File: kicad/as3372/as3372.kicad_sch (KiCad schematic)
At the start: 27 parts, among them J1 Conn_01x01, J2 Conn_01x02, J3 Conn_02x20_Odd_Even, U1 MUX508, U15 M24C02-WMN, U2 MUX508, U3 NE5532, U7 CAT9555YI-T2

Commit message: start placing
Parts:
- removed H2, H4: MountingHole, MountingHole:MountingHole_3.2mm_M3, symbol Mechanical:MountingHole
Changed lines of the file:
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@@
-    )
-  )
-  (symbol (lib_id "Mechanical:MountingHole") (at 360.68 38.1 0) (unit 1)
-    (in_bom yes) (on_board yes)
-    (property "Reference" "H4" (id 0) (at 363.22 36.9316 0)
-      (effects (font (size 1.27 1.27)) (justify left))
-    )
-    (property "Value" "MountingHole" (id 1) (at 363.22 39.243 0)
-      (effects (font (size 1.27 1.27)) (justify left))
-    )
-    (property "Footprint" "MountingHole:MountingHole_3.2mm_M3" (id 2) (at 360.68 38.1 0)
-      (effects (font (size 1.27 1.27)) hide)
-    )
-    (property "Datasheet" "~" (id 3) (at 360.68 38.1 0)
-      (effects (font (size 1.27 1.27)) hide)
-    )
-  )
-  (symbol (lib_id "Mechanical:MountingHole") (at 346.71 38.1 0) (unit 1)
-    (in_bom yes) (on_board yes)
-    (property "Reference" "H2" (id 0) (at 349.25 36.9316 0)
-      (effects (font (size 1.27 1.27)) (justify left))
-    )
-    (property "Value" "MountingHole" (id 1) (at 349.25 39.243 0)
-      (effects (font (size 1.27 1.27)) (justify left))
-    )
-    (property "Footprint" "MountingHole:MountingHole_3.2mm_M3" (id 2) (at 346.71 38.1 0)
-      (effects (font (size 1.27 1.27)) hide)
-    )
-    (property "Datasheet" "~" (id 3) (at 346.71 38.1 0)
-      (effects (font (size 1.27 1.27)) hide)
     )
   )
@@
       (reference "H1") (unit 1) (value "MountingHole") (footprint "MountingHole:MountingHole_3.2mm_M3")
     )
-    (path "/00000000-0000-0000-0000-0000640c295f"
-      (reference "H2") (unit 1) (value "MountingHole") (footprint "MountingHole:MountingHole_3.2mm_M3")
-    )
     (path "/00000000-0000-0000-0000-0000640c1f92"
       (reference "H3") (unit 1) (value "MountingHole") (footprint "MountingHole:MountingHole_3.2mm_M3")
     )
-    (path "/00000000-0000-0000-0000-0000640c239a"
-      (reference "H4") (unit 1) (value "MountingHole") (footprint "MountingHole:MountingHole_3.2mm_M3")
-    )
     (path "/3bdd9acf-e624-46b6-8487-c2e2595a6ff3"

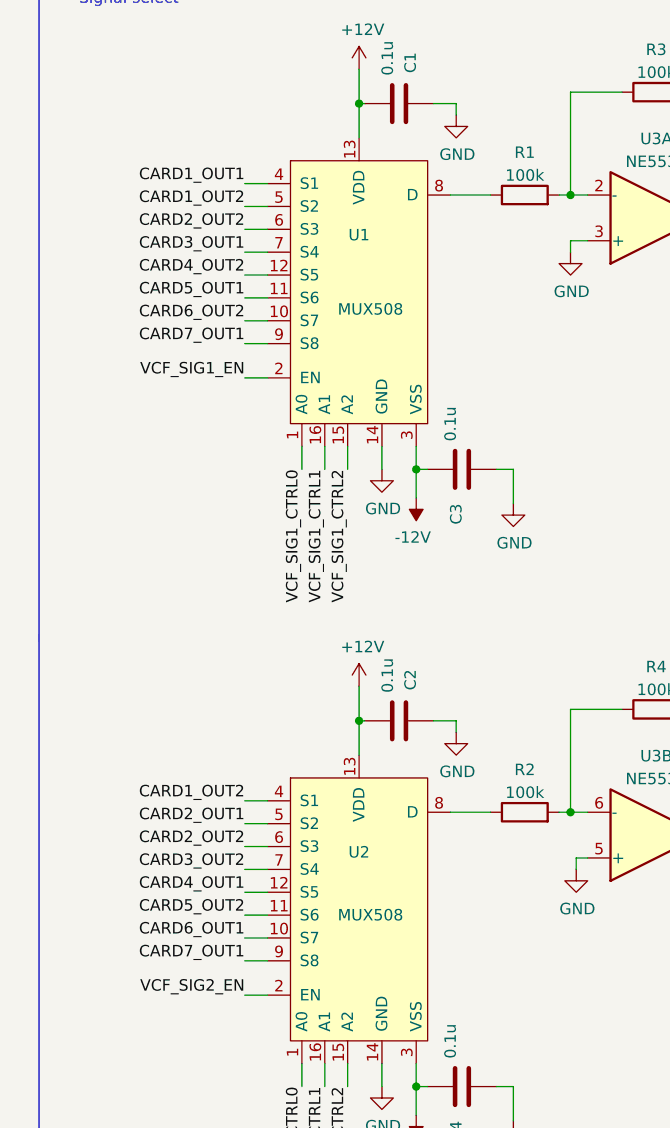
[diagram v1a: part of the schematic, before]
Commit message: having a tough time routing full filter with modes
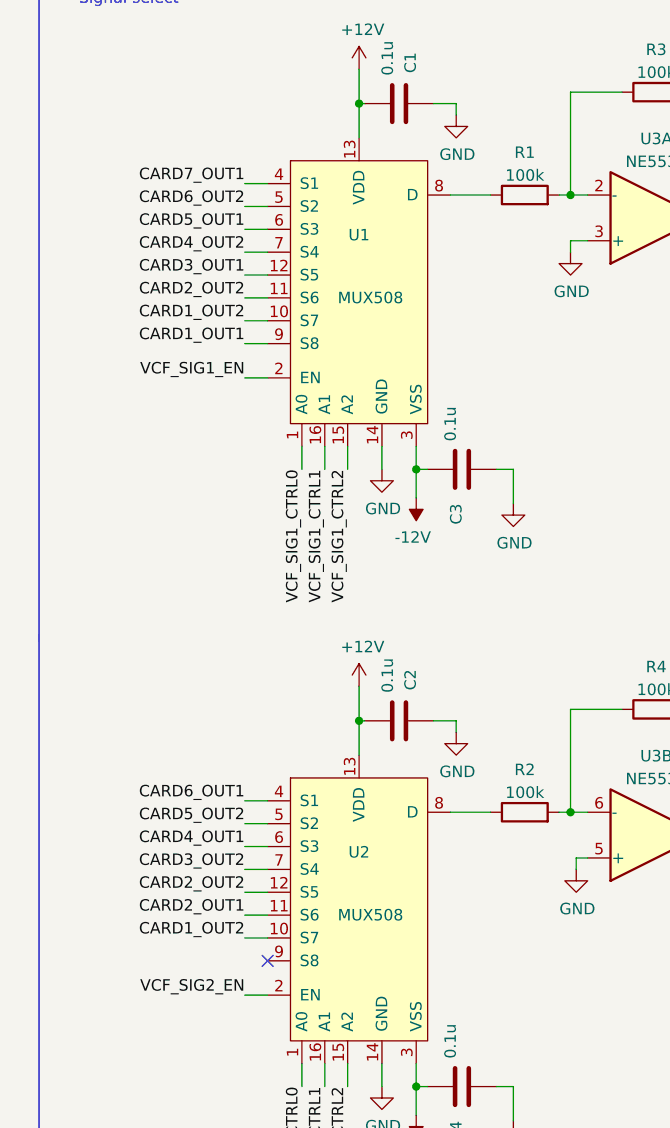
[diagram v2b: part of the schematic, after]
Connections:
- net CARD1_OUT1: now also U1.9 (S8); no longer U1.4 (S1)
- net CARD1_OUT2: now also U1.10 (S7), U2.10 (S7); no longer U1.5 (S2), U2.4 (S1)
- net CARD2_OUT1: now also U2.11 (S6); no longer U2.5 (S2)
- net CARD2_OUT2: now also U1.11 (S6), U2.12 (S5); no longer U1.6 (S3), U2.6 (S3)
- net CARD3_OUT1: now also U1.12 (S5); no longer U1.7 (S4)
- net CARD4_OUT1: now also U2.6 (S3); no longer U2.12 (S5)
- net CARD4_OUT2: now also U1.7 (S4); no longer U1.12 (S5)
- net CARD5_OUT1: now also U1.6 (S3); no longer U1.11 (S6)
- net CARD5_OUT2: now also U2.5 (S2); no longer U2.11 (S6)
- net CARD6_OUT1: now also U2.4 (S1); no longer U2.10 (S7)
- net CARD6_OUT2: now also U1.5 (S2); no longer U1.10 (S7)
- net CARD7_OUT1: now also U1.4 (S1); no longer U1.9 (S8), U2.9 (S8)
- no-connect marks 3 -> 4

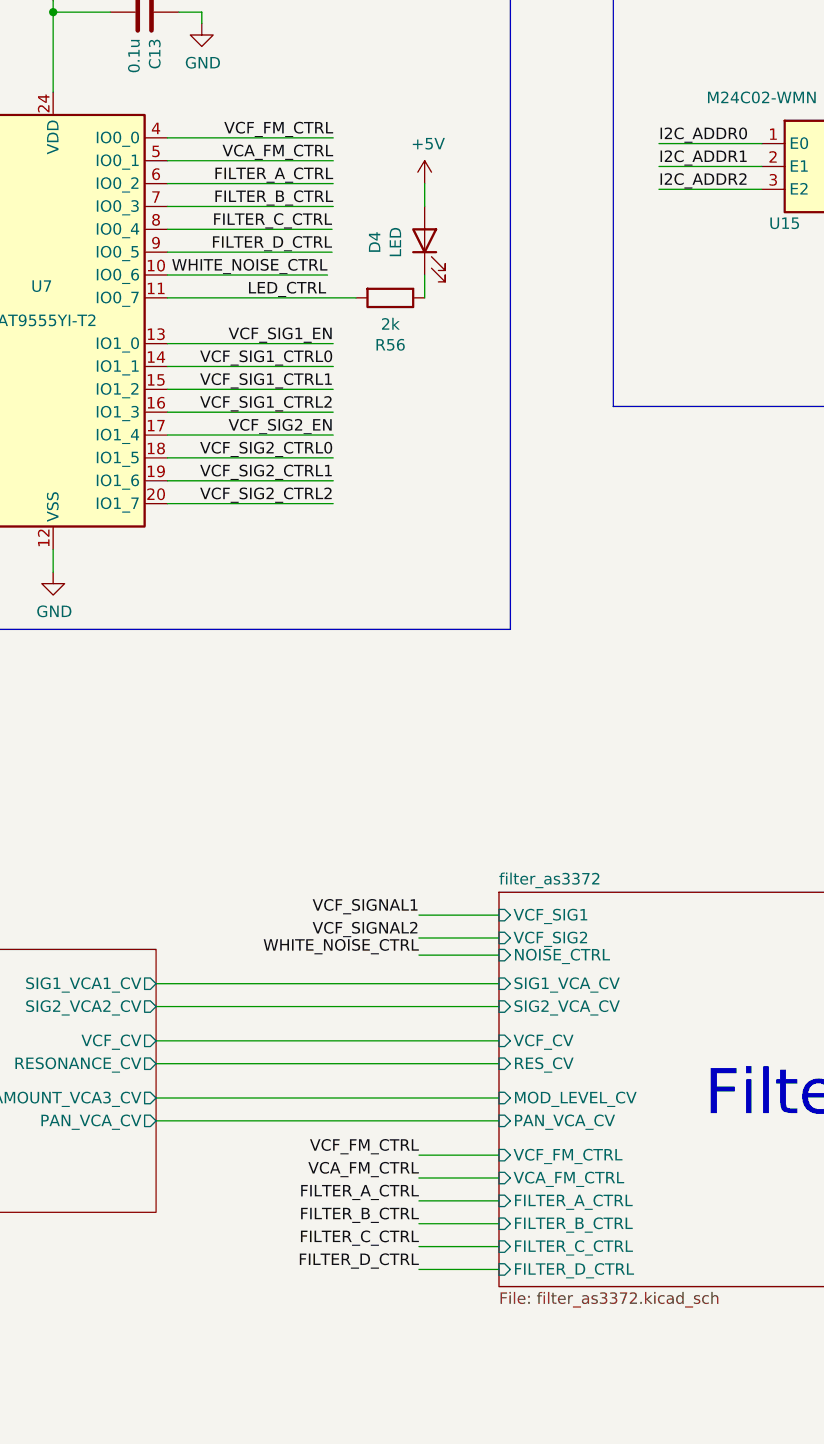
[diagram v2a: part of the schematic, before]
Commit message: simplify and remove filter mode select
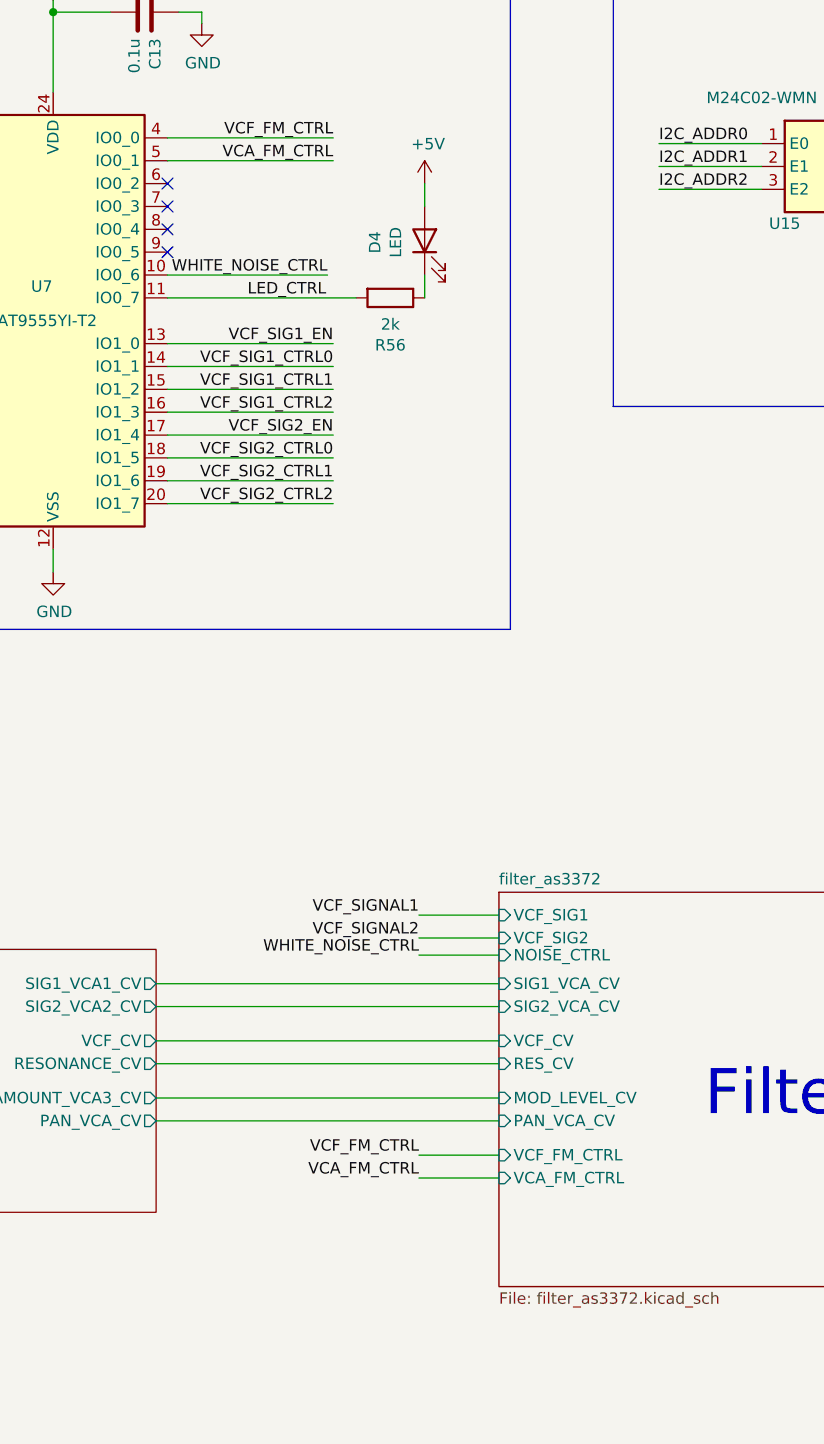
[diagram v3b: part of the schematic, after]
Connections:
- net FILTER_A_CTRL: no longer names the net of U7.6 (IO0_2)
- net FILTER_B_CTRL: no longer names the net of U7.7 (IO0_3)
- net FILTER_C_CTRL: no longer names the net of U7.8 (IO0_4)
- net FILTER_D_CTRL: no longer names the net of U7.9 (IO0_5)
- no-connect marks 4 -> 8
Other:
- sheet filter_as3372 ports: added none; removed FILTER_A_CTRL, FILTER_B_CTRL, FILTER_C_CTRL, FILTER_D_CTRL

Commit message: routing done needs review
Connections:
- net CARD1_OUT1: now also U2.9 (S8)
- net LED_CTRL: now also U7.6 (IO0_2); no longer U7.11 (IO0_7)
- no-connect marks 8 -> 7
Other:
- moved on the sheet: C1, C2, C3, C37, C4, C5, C6, D4, J1, J2, R1, R2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

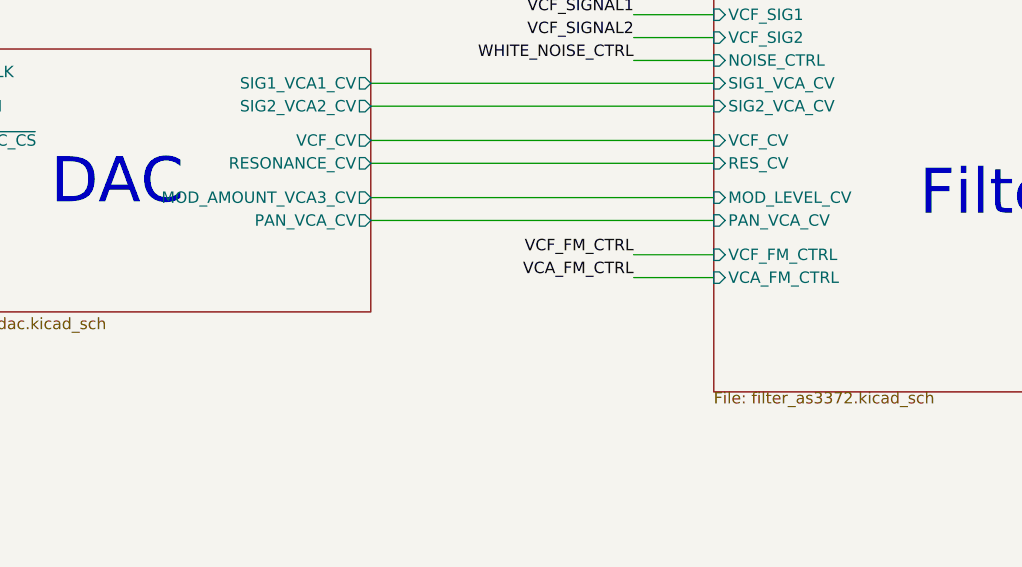
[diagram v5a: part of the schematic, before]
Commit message: add white noise enable/powerdown
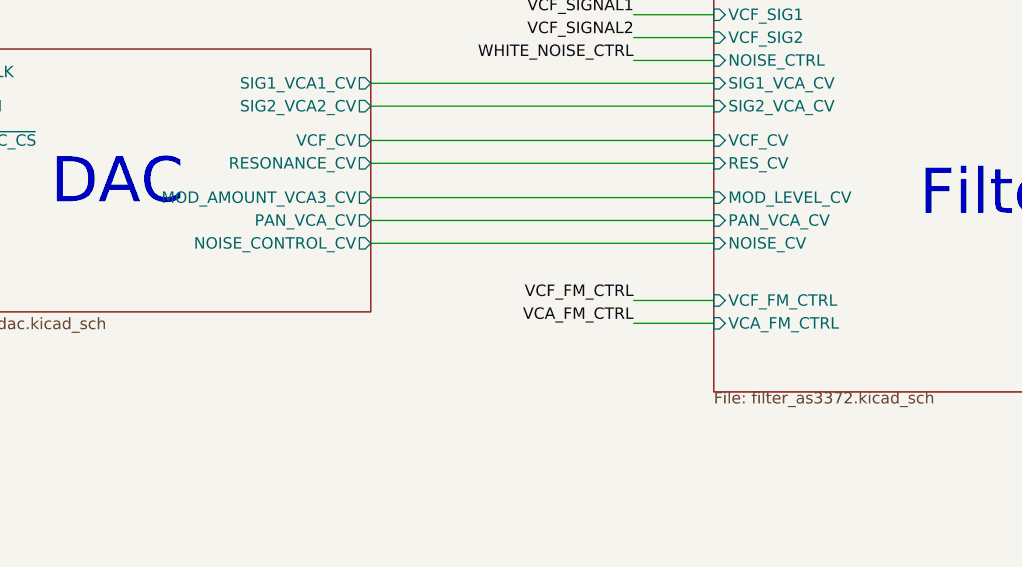
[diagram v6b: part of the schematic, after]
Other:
- sheet DAC ports: added NOISE_CONTROL_CV; removed none
- sheet filter_as3372 ports: added NOISE_CV; removed none
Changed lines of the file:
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@@
+    (stroke (width 0) (type default) (color 0 0 0 0))
+  )
+  (wire (pts (xy 191.77 156.21) (xy 229.87 156.21))
     (stroke (width 0) (type default) (color 0 0 0 0))
   )
@@
     (stroke (width 0) (type default) (color 0 0 0 0))
   )
-  (wire (pts (xy 220.98 157.48) (xy 229.87 157.48))
+  (wire (pts (xy 220.98 162.56) (xy 229.87 162.56))
     (stroke (width 0) (type default) (color 0 0 0 0))
   )
@@
     (stroke (width 0) (type default) (color 0 0 0 0))
   )
-  (wire (pts (xy 220.98 160.02) (xy 229.87 160.02))
+  (wire (pts (xy 220.98 165.1) (xy 229.87 165.1))
     (stroke (width 0) (type default) (color 0 0 0 0))
   )
@@
     (effects (font (size 1.27 1.27)) (justify right bottom))
   )
-  (label "VCF_FM_CTRL" (at 220.98 157.48 180)
+  (label "VCF_FM_CTRL" (at 220.98 162.56 180)
     (effects (font (size 1.27 1.27)) (justify right bottom))
   )
@@
     (effects (font (size 1.27 1.27)) (justify right bottom))
   )
-  (label "VCA_FM_CTRL" (at 220.98 160.02 180)
+  (label "VCA_FM_CTRL" (at 220.98 165.1 180)
     (effects (font (size 1.27 1.27)) (justify right bottom))
   )
@@
       (effects (font (size 1.27 1.27)) (justify right))
     )
+    (pin "NOISE_CONTROL_CV" output (at 191.77 156.21 0)
+      (effects (font (size 1.27 1.27)) (justify right))
+    )
   )
   (sheet (at 229.87 128.27) (size 64.77 44.45) (fields_autoplaced)
@@
       (effects (font (size 1.27 1.27)) (justify left))
     )
-    (pin "VCF_FM_CTRL" input (at 229.87 157.48 180)
-      (effects (font (size 1.27 1.27)) (justify left))
-    )
-    (pin "VCA_FM_CTRL" input (at 229.87 160.02 180)
+    (pin "VCF_FM_CTRL" input (at 229.87 162.56 180)
+      (effects (font (size 1.27 1.27)) (justify left))
+    )
+    (pin "VCA_FM_CTRL" input (at 229.87 165.1 180)
       (effects (font (size 1.27 1.27)) (justify left))
     )
@@
     )
     (pin "NOISE_CTRL" input (at 229.87 135.89 180)
+      (effects (font (size 1.27 1.27)) (justify left))
+    )
+    (pin "NOISE_CV" input (at 229.87 156.21 180)
       (effects (font (size 1.27 1.27)) (justify left))
     )
@@
       (reference "#PWR028") (unit 1) (value "GND") (footprint "")
     )
+    (path "/06519ee5-e3f7-4c1d-97d6-a8703fead30d/6ee86ae3-2656-4f63-9de6-e42b5b322983"
+      (reference "#PWR029") (unit 1) (value "GND") (footprint "")
+    )
     (path "/00000000-0000-0000-0000-000061ff2290/00000000-0000-0000-0000-0000622965dc"
       (reference "#PWR031") (unit 1) (value "+5V") (footprint "")
@@
       (reference "Q2") (unit 1) (value "MMBT3904") (footprint "Package_TO_SOT_SMD:SOT-23")
     )
+    (path "/06519ee5-e3f7-4c1d-97d6-a8703fead30d/55e53c3f-c971-4f19-922b-002bf51246f9"
+      (reference "Q3") (unit 1) (value "MMBT3904") (footprint "Package_TO_SOT_SMD:SOT-23")
+    )
     (path "/48ba0279-7271-4ec0-ba38-a30055ac9f59"
       (reference "R1") (unit 1) (value "100k") (footprint "Resistor_SMD:R_0402_1005Metric")
@@
       (reference "R15") (unit 1) (value "36k") (footprint "Resistor_SMD:R_0603_1608Metric")
     )
+    (path "/06519ee5-e3f7-4c1d-97d6-a8703fead30d/a9d46dee-3686-4e76-af83-0df79a10f957"
+      (reference "R16") (unit 1) (value "1k") (footprint "Resistor_SMD:R_0603_1608Metric")
+    )
     (path "/06519ee5-e3f7-4c1d-97d6-a8703fead30d/64293c9e-1637-4502-9e62-b413bb4bd05d"
       (reference "R18") (unit 1) (value "68k") (footprint "Resistor_SMD:R_0603_1608Metric")
@@
       (reference "TP13") (unit 1) (value "TestPoint") (footprint "TestPoint:TestPoint_Pad_2.0x2.0mm")
     )
-    (path "/00000000-0000-0000-0000-000061ff2290/a3ab1928-335f-4dcb-9beb-d7ee33a5ecd6"
-      (reference "TP14") (unit 1) (value "TestPoint") (footprint "TestPoint:TestPoint_Pad_2.0x2.0mm")
-    )
     (path "/06519ee5-e3f7-4c1d-97d6-a8703fead30d/802ac57d-6976-435d-bbe0-454dcb59ad4a"

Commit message: schematic updated
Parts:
- removed U3: NE5532, Package_SO:SOIC-8_3.9x4.9mm_P1.27mm, symbol Amplifier_Operational:NE5532
- added C21: 0.1u, Capacitor_SMD:C_0603_1608Metric, symbol Device:C
- added Q4: MMBT3904, Package_TO_SOT_SMD:SOT-23, symbol Transistor_BJT:MMBT3904
- added R17: 100, Resistor_SMD:R_0805_2012Metric, symbol Device:R
- added U3: TL074, Package_SO:SOIC-14_3.9x8.7mm_P1.27mm, symbol Amplifier_Operational:TL074
- R3, R4: value 100k -> 1k; footprint Resistor_SMD:R_0402_1005Metric -> Resistor_SMD:R_0805_2012Metric; LCSC Part C25741 -> C17513
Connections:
- net +12V: now also U3.4 (V+)
- net +5V: now also R4.2
- net -12V: now also U3.11 (V-)
- net GND: now also R1.1, R2.1, C21.2, Q4.2 (E), U3.12 (+)
- net GPIO_MODULE_DRIVEN: now also R17.2
- net VCF_SIGNAL1: now also U3.6 (-), U3.7; no longer R3.2
- net VCF_SIGNAL2: now also U3.1, U3.2 (-); no longer R4.2
- net at R3.1: now also U3.8, U3.9 (-); no longer R1.2
- net at R4.1: now also Q4.3 (C), R17.1; no longer R2.2
- net at U1.8 (D): now also R1.2, U3.5 (+); no longer R1.1
- net at U2.8 (D): now also R2.2, U3.3 (+); no longer R2.1
- new net: C21.1, Q4.1 (B), R3.2
- new net: U3.13 (-), U3.14
- new net VCF_RAW: U3.10 (+)
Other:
- sheet filter_as3372 ports: added VCF_RAW; removed none
- note added: "GPIO Module Driven: Take VCF output to drive a switch. Used to calibrate the noise source or resonanance level. And yes, it's inverted. You can do it. Cap gives a decent capability to detect via interrupt whether a signal is being generated or not. The diode is questionable..."
- note added: "Signal select -- output selected signal in-phase"
- note removed: "Signal select"
- moved on the sheet: R1, R2

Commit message: updates for v0.2
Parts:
- added H2, H4: MountingHole, MountingHole:MountingHole_3.2mm_M3, symbol Mechanical:MountingHole
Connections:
- net GND: now also U3.5 (+); no longer U3.12 (+)
- net VCA_FM_CTRL: now also U7.8 (IO0_4); no longer U7.5 (IO0_1)
- net VCF_SIGNAL1: now also U3.13 (-), U3.14; no longer U3.6 (-), U3.7
- net at R1.2, U1.8 (D): now also U3.12 (+); no longer U3.5 (+)
- new net: U3.6 (-), U3.7
- new net RES_FM_CTRL: U7.5 (IO0_1)
- no-connect marks 7 -> 6
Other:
- sheet filter_as3372 ports: added RES_FM_CTRL; removed none
